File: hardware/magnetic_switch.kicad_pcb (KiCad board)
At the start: 2 copper layers, 15 x 10 mm, 15 parts, among them J1 Conn_01x01_Socket, J2 Conn_01x01_Socket, J3 Conn_01x01_Socket, J4 Conn_01x01_Socket, Q1 SiA449DJ, Q2 BC847W, U1 DRV5012, U2 TPS70933

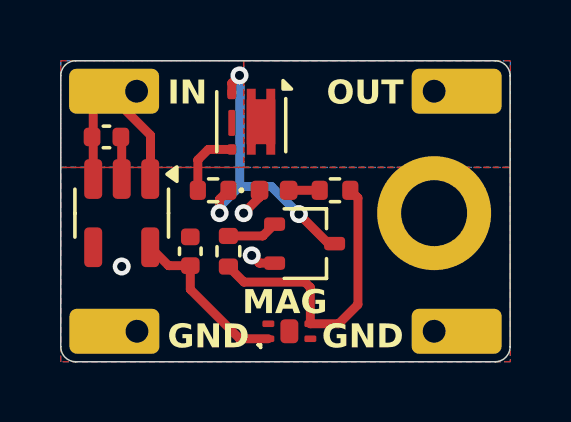
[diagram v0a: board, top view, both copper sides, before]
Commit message: Corrected issue with regulator enable pin which needs to be left floating, NOT tied to VCC and updated README to reflect the fact that testing is complete.
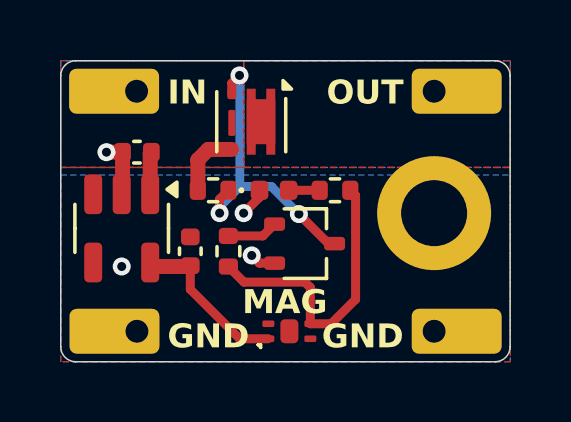
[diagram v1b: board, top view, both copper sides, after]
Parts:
- J1: value Conn_01x01_Socket -> V_IN
- J2: value Conn_01x01_Socket -> GND_IN
- J3: value Conn_01x01_Socket -> V_OUT
- J4: value Conn_01x01_Socket -> GND_OUT
- moved C2 1.14 mm to (140.7, 78.7), turned to 180 degrees
- moved U2 0.51 mm to (140.2, 81.3)
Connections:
- U2 pad 3: VDC -> unconnected-(U2-EN-Pad3)
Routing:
- net VDC: track 8.94 -> 4.33 mm
- net GND: track 3.25 -> 3.80 mm, vias 3 -> 4
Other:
- board text added: "1.0"
- board text added: "REV"
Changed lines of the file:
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@@
 	(net 8 "+VSW")
 	(net 9 "VDC")
+	(net 10 "unconnected-(U2-EN-Pad3)")
 	(footprint "Resistor_SMD:R_0402_1005Metric"
 		(layer "F.Cu")
@@
 			(pintype "passive")
 		)
-		(model "${KICAD8_3DMODEL_DIR}/Package_SON.3dshapes/WSON-8-1EP_2x2mm_P0.5mm_EP0.9x1.6mm.step"
+		(model "${KICAD8_3DMODEL_DIR}/Package_SON.3dshapes/WSON-6-1EP_2x2mm_P0.65mm_EP1x1.6mm.wrl"
 			(offset
 				(xyz 0 0 0)
@@
 	(footprint "Capacitor_SMD:C_0402_1005Metric"
 		(layer "F.Cu")
-		(at 139.7 78.232)
+		(at 140.716 78.74 180)
 		(descr "Capacitor SMD 0402 (1005 Metric), square (rectangular) end terminal, IPC_7351 nominal, (Body size source: IPC-SM-782 page 76, https://www.pcb-3d.com/wordpress/wp-content/uploads/ipc-sm-782a_amendment_1_and_2.pdf), generated with kicad-footprint-generator")
 		(tags "capacitor")
 		(property "Reference" "C2"
-			(at 0 -1.16 0)
+			(at 0 -1.16 360)
 			(layer "F.SilkS")
 			(hide yes)
@@
 		)
 		(property "Value" "2u2"
-			(at 0 1.16 0)
+			(at 0 1.16 360)
 			(layer "F.Fab")
 			(effects
@@
 		)
 		(property "Footprint" "Capacitor_SMD:C_0402_1005Metric"
-			(at 0 0 0)
+			(at 0 0 180)
 			(unlocked yes)
 			(layer "F.Fab")
@@
 		)
 		(property "Datasheet" ""
-			(at 0 0 0)
+			(at 0 0 180)
 			(unlocked yes)
 			(layer "F.Fab")
@@
 		)
 		(property "Description" "Unpolarized capacitor, small symbol"
-			(at 0 0 0)
+			(at 0 0 180)
 			(unlocked yes)
 			(layer "F.Fab")
@@
 		(attr smd)
 		(fp_line
-			(start -0.107836 -0.36)
-			(end 0.107836 -0.36)
+			(start -0.107836 0.36)
+			(end 0.107836 0.36)
 			(stroke
 				(width 0.12)
@@
 		)
 		(fp_line
-			(start -0.107836 0.36)
-			(end 0.107836 0.36)
+			(start -0.107836 -0.36)
+			(end 0.107836 -0.36)
 			(stroke
 				(width 0.12)
@@
 		)
 		(fp_line
-			(start -0.91 -0.46)
-			(end 0.91 -0.46)
+			(start 0.91 0.46)
+			(end -0.91 0.46)
 			(stroke
 				(width 0.05)
@@
 		)
 		(fp_line
-			(start -0.91 0.46)
-			(end -0.91 -0.46)
+			(start 0.91 -0.46)
+			(end 0.91 0.46)
 			(stroke
 				(width 0.05)
@@
 		)
 		(fp_line
-			(start 0.91 -0.46)
-			(end 0.91 0.46)
+			(start -0.91 0.46)
+			(end -0.91 -0.46)
 			(stroke
 				(width 0.05)
@@
 		)
 		(fp_line
-			(start 0.91 0.46)
-			(end -0.91 0.46)
+			(start -0.91 -0.46)
+			(end 0.91 -0.46)
 			(stroke
 				(width 0.05)
@@
 		)
 		(fp_line
-			(start -0.5 -0.25)
-			(end 0.5 -0.25)
+			(start 0.5 0.25)
+			(end -0.5 0.25)
 			(stroke
 				(width 0.1)
@@
 		)
 		(fp_line
-			(start -0.5 0.25)
-			(end -0.5 -0.25)
+			(start 0.5 -0.25)
+			(end 0.5 0.25)
 			(stroke
 				(width 0.1)
@@
 		)
 		(fp_line
-			(start 0.5 -0.25)
-			(end 0.5 0.25)
+			(start -0.5 0.25)
+			(end -0.5 -0.25)
 			(stroke
 				(width 0.1)
@@
 		)
 		(fp_line
-			(start 0.5 0.25)
-			(end -0.5 0.25)
+			(start -0.5 -0.25)
+			(end 0.5 -0.25)
 			(stroke
 				(width 0.1)
@@
 		)
 		(fp_text user "${REFERENCE}"
-			(at 0 0 0)
+			(at 0 0 360)
 			(layer "F.Fab")
 			(effects
@@
 		)
 		(pad "1" smd roundrect
-			(at -0.48 0)
+			(at -0.48 0 180)
 			(size 0.56 0.62)
 			(layers "F.Cu" "F.Paste" "F.Mask")
@@
 		)
 		(pad "2" smd roundrect
-			(at 0.48 0)
+			(at 0.48 0 180)
 			(size 0.56 0.62)
 			(layers "F.Cu" "F.Paste" "F.Mask")
@@
 			)
 		)
-		(property "Value" "Conn_01x01_Socket"
+		(property "Value" "V_OUT"
 			(at 0 1 180)
 			(unlocked yes)
@@
 			)
 		)
-		(property "Value" "Conn_01x01_Socket"
+		(property "Value" "V_IN"
 			(at 0 1 0)
 			(unlocked yes)
@@
 			)
 		)
-		(property "Value" "Conn_01x01_Socket"
+		(property "Value" "GND_OUT"
 			(at 0 1 180)
 			(unlocked yes)
@@
 		(sheetname "Root")
 		(sheetfile "magnetic_switch.kicad_sch")
+		(clearance 0.5)
 		(attr exclude_from_pos_files exclude_from_bom)
 		(fp_circle
@@
 	(footprint "Package_TO_SOT_SMD:SOT-23-5"
 		(layer "F.Cu")
-		(at 140.208 80.772 -90)
+		(at 140.208 81.28 -90)
 		(descr "SOT, 5 Pin (https://www.jedec.org/sites/default/files/docs/Mo-178c.PDF variant AA), generated with kicad-footprint-generator ipc_gullwing_generator.py")
 		(tags "SOT TO_SOT_SMD")
@@
 			(layers "F.Cu" "F.Paste" "F.Mask")
 			(roundrect_rratio 0.25)
-			(net 9 "VDC")
+			(net 10 "unconnected-(U2-EN-Pad3)")
 			(pinfunction "EN")
-			(pintype "input")
+			(pintype "input+no_connect")
 		)
 		(pad "4" smd roundrect
@@
 			)
 		)
-		(property "Value" "Conn_01x01_Socket"
+		(property "Value" "GND_IN"
 			(at 0 1 0)
 			(unlocked yes)
@@
 		(layer "Edge.Cuts")
 	)
+	(gr_text "REV"
+		(at 149.098 77.978 0)
+		(layer "B.SilkS")
+		(effects
+			(font
+				(size 0.7 0.7)
+				(thickness 0.12)
+				(bold yes)
+			)
+			(justify left bottom mirror)
+		)
+	)
 	(gr_text "Magnet\n"
 		(at 148.082 84.201 0)
@@
 		)
 	)
+	(gr_text "1.0"
+		(at 147.066 77.978 0)
+		(layer "B.SilkS")
+		(effects
+			(font
+				(size 0.7 0.7)
+				(thickness 0.12)
+				(bold yes)
+			)
+			(justify left bottom mirror)
+		)
+	)
 	(gr_text "IN\n"
 		(at 141.732 77.216 0)
@@
 	)
 	(segment
-		(start 140.208 78.232)
-		(end 140.208 79.6345)
-		(width 0.3)
+		(start 140.236 80.1145)
+		(end 140.208 80.1425)
+		(width 0.5)
 		(layer "F.Cu")
 		(net 1)
@@
 	)
 	(segment
+		(start 139.7 78.74)
+		(end 140.236 78.74)
+		(width 0.5)
+		(layer "F.Cu")
+		(net 1)
+	)
+	(segment
+		(start 140.236 78.74)
+		(end 140.236 80.1145)
+		(width 0.5)
+		(layer "F.Cu")
+		(net 1)
+	)
+	(segment
 		(start 144.79774 82.438)
 		(end 145.304 82.438)
@@
 		(net 1)
 	)
+	(via
+		(at 139.7 78.74)
+		(size 0.6)
+		(drill 0.3)
+		(layers "F.Cu" "B.Cu")
+		(free yes)
+		(net 1)
+	)
 	(segment
 		(start 145.773 80.01)
@@
 	)
 	(segment
-		(start 147.828 80.01)
-		(end 148.082 80.264)
+		(start 146.496 84.459)
+		(end 147.189 84.459)
 		(width 0.3)
 		(layer "F.Cu")
@@
 	)
 	(segment
-		(start 147.443 84.459)
-		(end 146.496 84.459)
-		(width 0.3)
-		(layer "F.Cu")
-		(net 5)
-	)
-	(segment
 		(start 144.282 83.07)
 		(end 146.316 83.07)
@@
 	)
 	(segment
-		(start 148.082 80.264)
-		(end 148.082 83.82)
+		(start 147.189 84.459)
+		(end 148.004 83.644)
 		(width 0.3)
 		(layer "F.Cu")
@@
 	)
 	(segment
-		(start 143.764 82.552)
-		(end 144.282 83.07)
+		(start 148.004 83.644)
+		(end 148.004 80.186)
 		(width 0.3)
 		(layer "F.Cu")
@@
 	)
 	(segment
-		(start 148.082 83.82)
-		(end 147.443 84.459)
+		(start 143.764 82.552)
+		(end 144.282 83.07)
 		(width 0.3)
 		(layer "F.Cu")
@@
 	)
 	(segment
-		(start 144.141 84.959)
-		(end 145.096 84.959)
+		(start 148.004 80.186)
+		(end 147.828 80.01)
 		(width 0.3)
 		(layer "F.Cu")
-		(net 7)
+		(net 5)
 	)
 	(segment
-		(start 141.7705 82.522)
-		(end 141.158 81.9095)
-		(width 0.3)
+		(start 141.2905 82.55)
+		(end 142.466 82.55)
+		(width 0.5)
 		(layer "F.Cu")
 		(net 7)
 	)
 	(segment
-		(start 142.494 82.522)
-		(end 141.7705 82.522)
+		(start 144.141 84.959)
+		(end 145.096 84.959)
 		(width 0.3)
 		(layer "F.Cu")
@@
 	)
 	(segment
-		(start 139.258 77.15)
-		(end 139.7 76.708)
-		(width 0.3)
+		(start 141.158 82.4175)
+		(end 141.2905 82.55)
+		(width 0.5)
 		(layer "F.Cu")
-		(net 9)
+		(net 7)
 	)
 	(segment
-		(start 141.158 79.6345)
-		(end 141.168 79.6245)
-		(width 0.3)
+		(start 142.466 82.55)
+		(end 142.494 82.522)
+		(width 0.5)
 		(layer "F.Cu")
-		(net 9)
+		(net 7)
 	)
 	(segment
-		(start 139.258 79.6345)
-		(end 139.258 77.15)
-		(width 0.3)
+		(start 142.746 80.01)
+		(end 142.746 78.996)
+		(width 0.5)
 		(layer "F.Cu")
 		(net 9)
 	)
 	(segment
-		(start 143.093 78.649)
-		(end 143.876 78.649)
+		(start 139.258 77.15)
+		(end 139.7 76.708)
 		(width 0.3)
 		(layer "F.Cu")
@@
 	)
 	(segment
-		(start 141.168 78.176)
-		(end 139.7 76.708)
-		(width 0.3)
+		(start 141.158 78.778)
+		(end 141.196 78.74)
+		(width 0.5)
 		(layer "F.Cu")
 		(net 9)
 	)
 	(segment
-		(start 141.168 79.6245)
-		(end 141.168 78.176)
-		(width 0.3)
+		(start 141.158 80.1425)
+		(end 141.158 78.778)
+		(width 0.5)
 		(layer "F.Cu")
 		(net 9)
 	)
 	(segment
-		(start 142.746 80.01)
-		(end 142.746 78.996)
-		(width 0.3)
+		(start 142.746 78.996)
+		(end 143.093 78.649)
+		(width 0.5)
 		(layer "F.Cu")
 		(net 9)
 	)
 	(segment
-		(start 142.746 78.996)
-		(end 143.093 78.649)
-		(width 0.3)
+		(start 143.093 78.649)
+		(end 143.876 78.649)
+		(width 0.5)
 		(layer "F.Cu")
 		(net 9)
@@
 		(layer "F.Cu")
 		(hatch edge 0.5)
-		(priority 1)
+		(priority 2)
 		(connect_pads yes
 			(clearance 0.25)
@@
 		(polygon
 			(pts
-				(xy 138.176 79.248) (xy 153.162 79.248) (xy 153.162 85.725) (xy 138.176 85.725)
+				(xy 138.176 79.502) (xy 153.162 79.502) (xy 153.162 85.725) (xy 138.176 85.725)
 			)
 		)

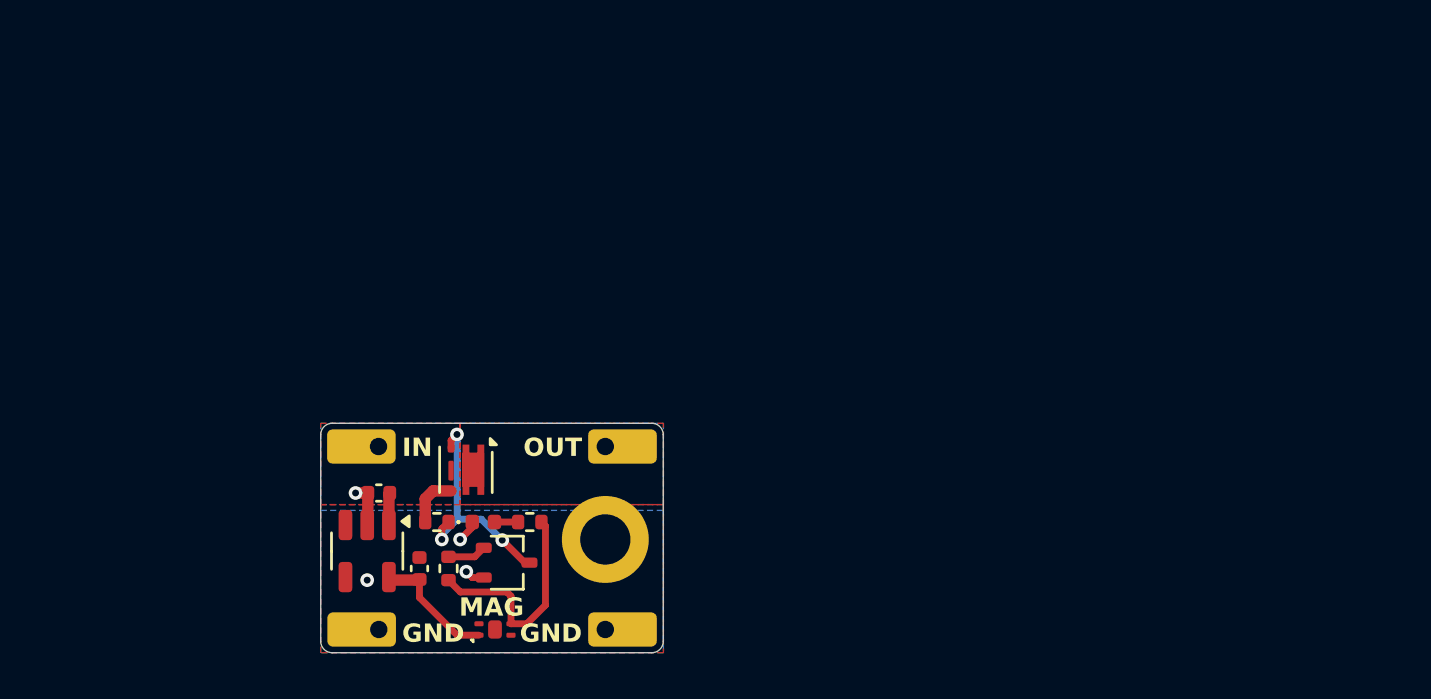
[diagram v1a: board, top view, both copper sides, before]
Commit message: updated to smaller components and re-layed out.
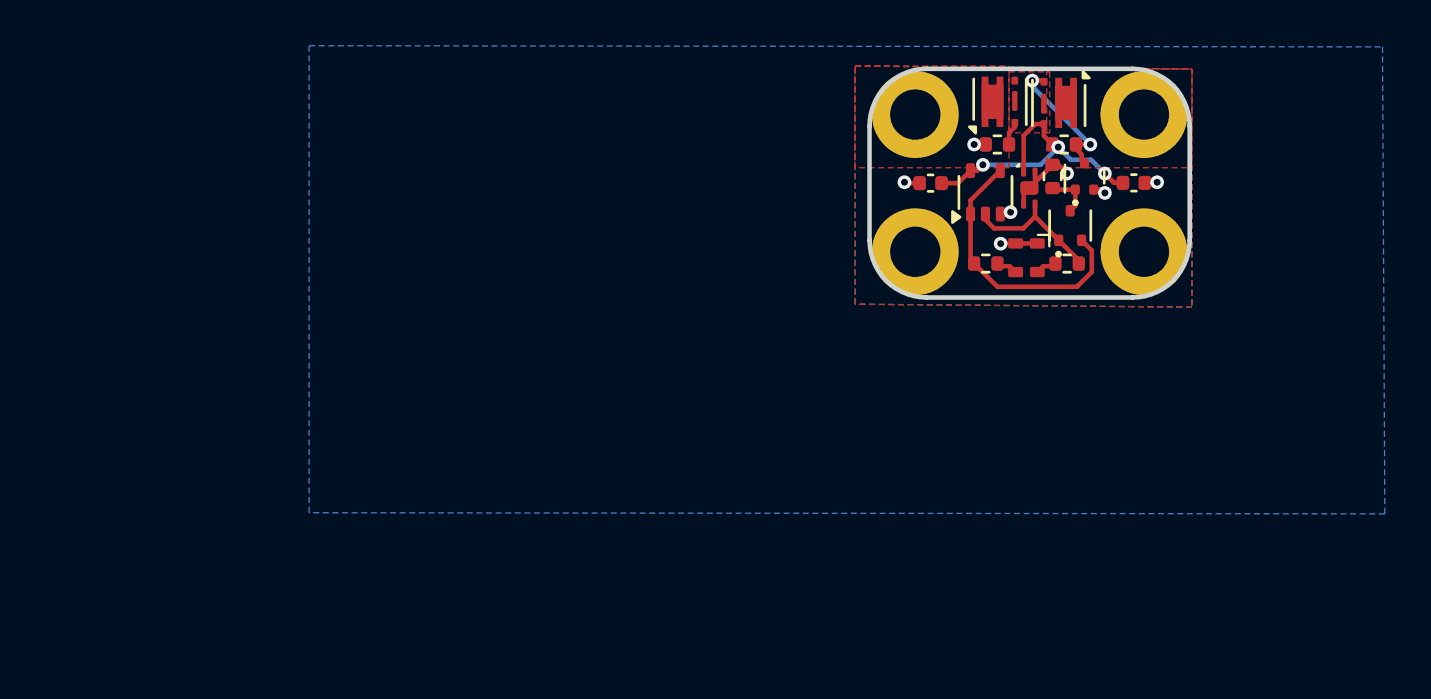
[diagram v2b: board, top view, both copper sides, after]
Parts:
- removed H1: MountingHole, MountingHole:MountingHole_2.2mm_M2_DIN965_Pad
- removed Q2: BC847W, Package_TO_SOT_SMD:SOT-323_SC-70
- removed R3: 1k, Resistor_SMD:R_0402_1005Metric
- added D3: BAT54CT, Package_TO_SOT_SMD:SOT-523, F.Cu at (170.9, 67.0)
- added Q3: SiA449DJ, Package_TO_SOT_SMD:Vishay_PowerPAK_SC70-6L_Single, F.Cu at (170.4, 61.7)
- added Q4: RUM002N02T2L, Package_TO_SOT_SMD:SOT-723, F.Cu at (171.6, 64.9)
- added R4: 1k, Resistor_SMD:R_0402_1005Metric, F.Cu at (167.3, 68.7)
- added R5: 100k, Resistor_SMD:R_0402_1005Metric, F.Cu at (170.7, 63.5)
- added R6: 100k, Resistor_SMD:R_0402_1005Metric, F.Cu at (170.2, 64.9)
- C2: value 2u2 -> 100n
- D1: value RED_LED -> XL-1615SURUGC; footprint LED_SMD:LED_0402_1005Metric -> Footprints:LED_SMT_DUAL_1615
- J1, J2, J3, J4: footprint My Footprints:WireSolderPad_w_hole -> MountingHole:MountingHole_2.2mm_M2_DIN965_Pad
- R1: value 1k -> 100k
- R2: value 100k -> 1k
- U1: footprint My Footprints:X2SON_4_EP -> Footprints:X2SON_4_EP
- U2: value TPS70933 -> 74LVC1G80; footprint Package_TO_SOT_SMD:SOT-23-5 -> Package_TO_SOT_SMD:SOT-353_SC-70-5
- moved C1 35.5 mm to (173.7, 65.2), turned to 0 degrees
- moved U2 31.3 mm to (167.2, 65.6), turned to 90 degrees
- moved U1 30.3 mm to (169.2, 65.4), turned to 0 degrees
- moved R2 29.8 mm to (170.8, 68.7)
- moved J4 28.8 mm to (174.2, 68.2), turned to 0 degrees
- moved J2 28.7 mm to (164.2, 68.2)
- moved Q1 28.4 mm to (167.9, 61.6), turned to 90 degrees
- moved C2 27.7 mm to (164.8, 65.2)
- moved J3 27.7 mm to (174.2, 62.2), turned to 0 degrees
- moved J1 27.6 mm to (164.2, 62.2)
- moved D1 26.4 mm to (169.0, 68.5), turned to -90 degrees
- moved R1 26.3 mm to (167.8, 63.5), turned to 180 degrees
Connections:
- C1 pad 1: +3V3 -> VDC
- D1 pad 2: Net-(D1-A) -> GND
- J1 pad 1: VDC -> +BATT
- Q1 pad 1: +VSW -> +BATT
- R1 pad 1: Net-(D1-A) -> Net-(Q1-G)
- R1 pad 2: Net-(U1-OUT) -> GND
- R2 pad 1: VDC -> Net-(D1-A2)
- R2 pad 2: Net-(Q1-G) -> /HALL_OUT
- U1 pad 1: +3V3 -> VDC
- U1 pad 3: Net-(U1-OUT) -> /HALL_OUT
- U2 pad 1: VDC -> Net-(U2-D)
- U2 pad 2: GND -> /HALL_OUT
- U2 pad 3: unconnected-(U2-EN-Pad3) -> GND
- U2 pad 4: unconnected-(U2-NC-Pad4) -> Net-(U2-D)
- U2 pad 5: +3V3 -> VDC
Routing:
- net Net-(U2-D): track 0.00 -> 12.1 mm
- net Net-(U1-OUT): track 9.78 -> 0.00 mm
- net Net-(Q1-G): track 10.5 -> 1.04 mm, vias 3 -> 0
- net VDC: track 4.33 -> 13.0 mm, vias 0 -> 3
- net /HALL_OUT: track 0.00 -> 6.18 mm
- net Net-(Q3-G): track 0.00 -> 5.99 mm, vias 0 -> 2
- net +3V3: track 5.48 -> 0.00 mm
- net GND: track 3.80 -> 8.21 mm, vias 4 -> 7
- net Net-(D3-K): track 0.00 -> 2.05 mm
- net Net-(Q2-B): track 1.70 -> 0.00 mm
- net Net-(D1-A): track 1.03 -> 0.00 mm
- net Net-(D1-A2): track 0.00 -> 0.95 mm
- net Net-(D1-A1): track 0.00 -> 0.95 mm
- added copper zone on F.Cu, net +BATT
- removed copper zone on B.Cu, net +VSW
- removed copper zone on B.Cu, net VDC
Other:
- board size 15 x 10 mm -> 14 x 10 mm
- board text removed: "1.0"
- board text removed: "GND"
- board text removed: "IN"
- board text removed: "MAG"
- board text removed: "Magnet"
- board text removed: "OUT"
- board text removed: "REV"

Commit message: added a linear regulator to allow up to +12V input. This version was sent for manufacture.
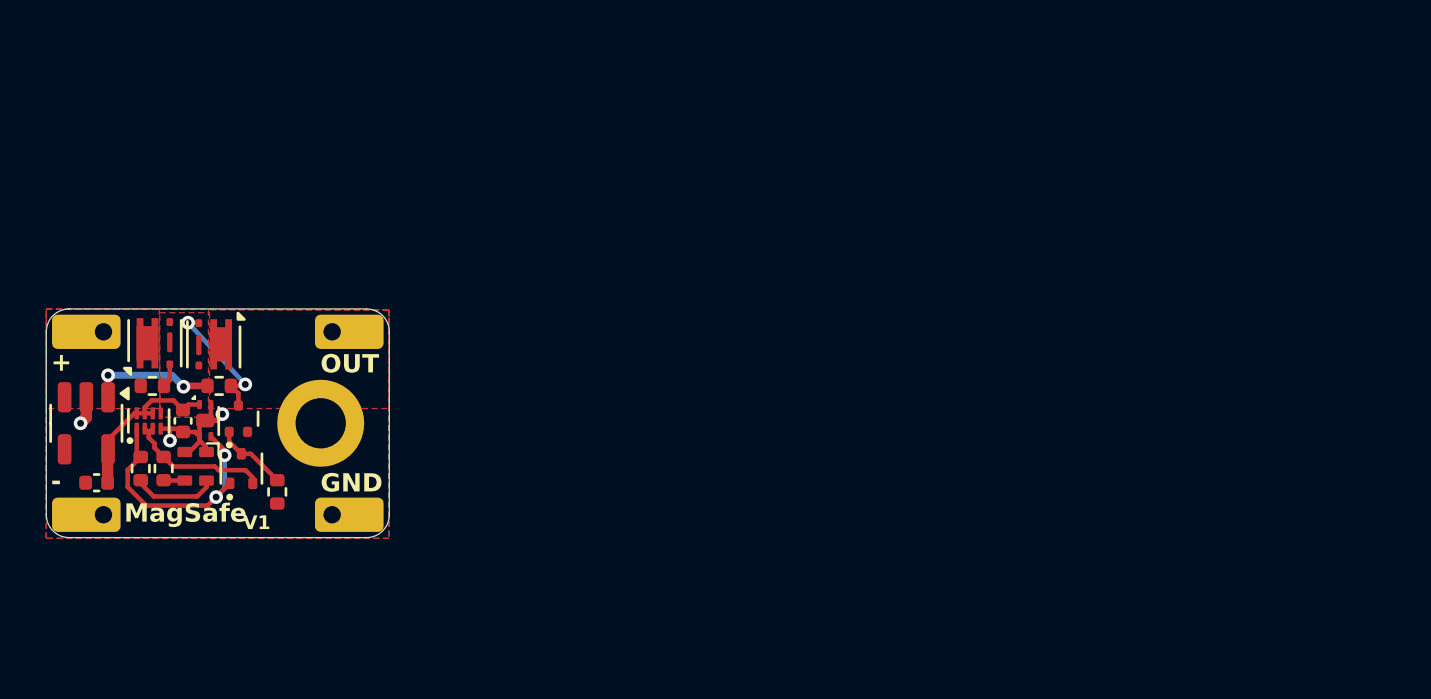
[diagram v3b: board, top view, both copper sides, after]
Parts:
- removed U2: 74LVC1G80, Package_TO_SOT_SMD:SOT-353_SC-70-5
- added H1: MountingHole_Pad, MountingHole:MountingHole_2.2mm_M2_DIN965_Pad, F.Cu at (138.2, 75.7)
- added U3: TPS70933, Package_TO_SOT_SMD:SOT-23-5, F.Cu at (127.9, 75.7)
- added U4: SN74AUP1G74, Package_SON:X2SON-8_1.4x1mm_P0.35mm, F.Cu at (130.7, 75.6)
- J1, J2, J3, J4: footprint MountingHole:MountingHole_2.2mm_M2_DIN965_Pad -> Footprints:WireSolderPad_w_hole
- Q1, Q3: value SiA449DJ -> DMP2040UFDF
- moved C1 47.2 mm to (128.4, 78.3), turned to 180 degrees
- moved R2 41.5 mm to (130.3, 77.7), turned to 90 degrees
- moved Q4 38.5 mm to (134.6, 75.5)
- moved Q1 38.4 mm to (130.9, 72.2)
- moved Q3 38.4 mm to (133.5, 72.2)
- moved R1 38.4 mm to (130.8, 74.1)
- moved R5 38.4 mm to (133.7, 74.1)
- moved D3 37.8 mm to (134.7, 77.7)
- moved D1 37.5 mm to (132.7, 77.6)
- moved U1 37.4 mm to (133.1, 75.6)
- moved J2 37.3 mm to (128.7, 79.7)
- moved J4 37.3 mm to (138.7, 79.7), turned to 180 degrees
- moved R4 37.1 mm to (131.3, 77.7), turned to 90 degrees
- moved J1 36.7 mm to (128.7, 71.7)
- moved J3 36.7 mm to (138.7, 71.7), turned to 180 degrees
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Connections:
- C1 pad 1: VDC -> +3V3
- C2 pad 1: VDC -> +3V3
- Q1 pad 4: VDC -> Net-(Q1-S)
- Q3 pad 4: VDC -> Net-(Q1-S)
- R5 pad 1: VDC -> Net-(Q1-S)
- U1 pad 1: VDC -> +3V3
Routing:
- net VDC: track 13.0 -> 0.00 mm, vias 3 -> 0
- net +3V3: track 0.00 -> 7.33 mm
- net Net-(U4-D): track 12.1 -> 6.35 mm
- net Net-(Q1-S): track 0.00 -> 5.53 mm, vias 0 -> 2
- net /HALL_OUT: track 6.18 -> 11.1 mm, vias 0 -> 2
- net Net-(D1-A2): track 0.95 -> 3.71 mm
- net Net-(D3-K): track 2.05 -> 3.23 mm
- net GND: track 8.21 -> 7.94 mm, vias 7 -> 3
- added copper zone on F.Cu, net Net-(Q1-S)
- removed copper zone on F.Cu, net VDC
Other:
- board size 14 x 10 mm -> 15 x 10 mm
- board text added: "+"
- board text added: "-"
- board text added: "GND"
- board text added: "MagSafe"
- board text added: "OUT"
- board text added: "V1"
